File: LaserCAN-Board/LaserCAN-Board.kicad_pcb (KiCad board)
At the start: 4 copper layers, 25 x 25 mm, 48 parts, among them J2 TC2050-IDC-NL, U1 NCP730BMT330TBG, U2 VL53L1CXV0FY1, U3 M24C64-RMN6TP, U4 STM32F103C8Tx, U5 USBLC6-2P6, U6 SN65HVD230, U7 USBLC6-2P6, U8 AP62200TWU-7

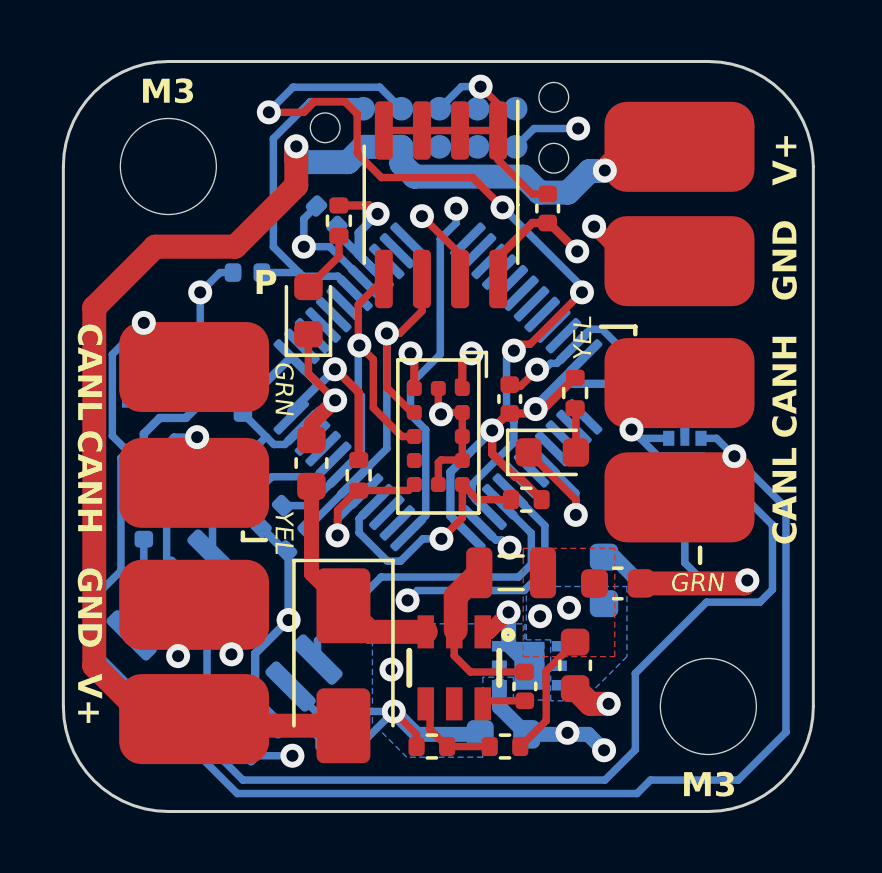
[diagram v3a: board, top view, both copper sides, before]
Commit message: Add new power regulation, completely re-route board to accomodate
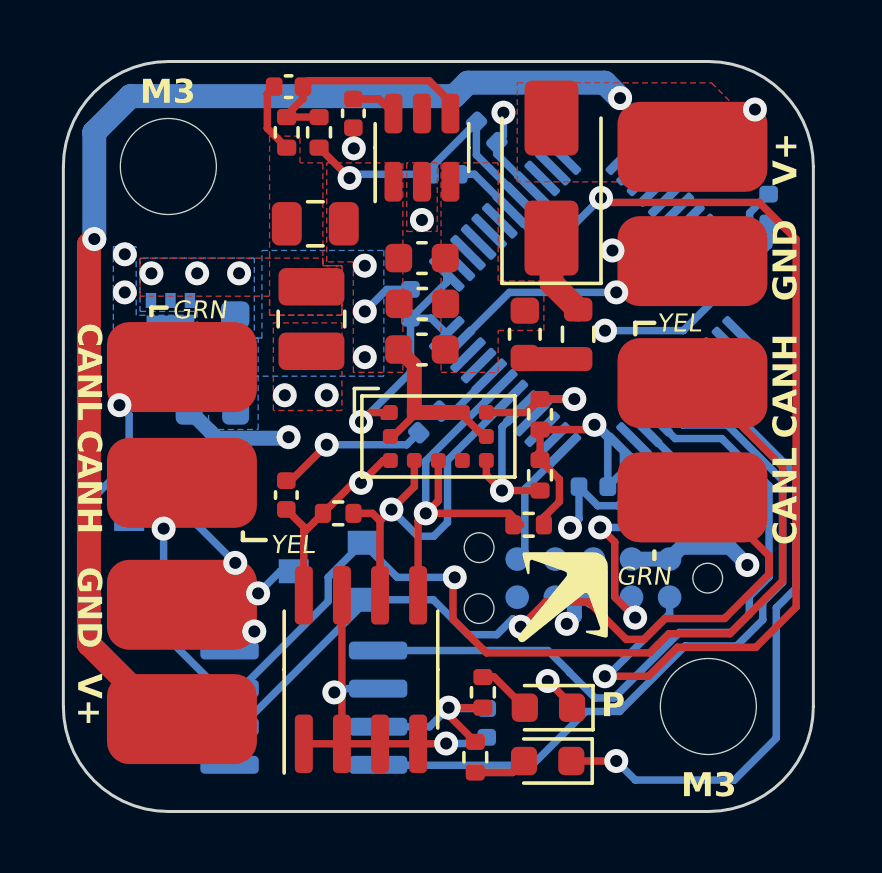
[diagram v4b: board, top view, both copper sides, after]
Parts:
- removed C10, C11, C14: 100n, Capacitor_SMD:C_0402_1005Metric
- removed C15: 10uF, Capacitor_SMD:C_0603_1608Metric
- removed L1: 4.7uH, Inductor_SMD:L_0805_2012Metric
- removed U5, U7: USBLC6-2P6, Package_TO_SOT_SMD:SOT-666
- removed U8: AP62200TWU-7, AP62200TWU-7:TSOT-26_L2.9-W1.6-P0.95-LS2.8-BL
- added C16: 10uF, Capacitor_SMD:C_0603_1608Metric, F.Cu at (132.0, 106.6)
- added C17: 10uF, Capacitor_SMD:C_0603_1608Metric, F.Cu at (132.0, 108.1)
- added C18: 100n, Capacitor_SMD:C_0402_1005Metric, F.Cu at (129.7, 101.7)
- added C19: 22uF, Capacitor_SMD:C_0805_2012Metric, F.Cu at (128.4, 105.4)
- added D4: PESD1CAN,215, PESD1CAN:SOT-23_L2.9-W1.3-P1.90-LS2.4-BR, B.Cu at (123.3, 114.3)
- added D5: PESD1CAN,215, PESD1CAN:SOT-23_L2.9-W1.3-P1.90-LS2.4-BR, B.Cu at (128.8, 117.0)
- added FB1: BLM18AG102SN1D, Inductor_SMD:L_0603_1608Metric, F.Cu at (135.4, 109.1)
- added L2: 22uH, Inductor_SMD:L_1008_2520Metric, F.Cu at (128.3, 108.6)
- added R9: 4.7 100mW, Resistor_SMD:R_0603_1608Metric, F.Cu at (137.2, 109.1)
- added U9: TPS54202DDC, Package_TO_SOT_SMD:SOT-23-6, F.Cu at (132.0, 102.9)
- C13: value 10uF -> 33pF; footprint Capacitor_SMD:C_0603_1608Metric -> Capacitor_SMD:C_0402_1005Metric
- C8: moved to B.Cu
- D1: value D_Schottky -> SS14
- G***, R3, R4: moved to F.Cu
- R2: value 41k 1% -> 100k
- R8: value 10k 1% -> 18.2k
- moved R2 21.7 mm to (127.4, 102.4), turned to 90 degrees
- moved R8 20.8 mm to (128.5, 102.4), turned to -90 degrees
- moved C13 19.9 mm to (127.5, 100.8)
- moved J2 19.2 mm to (140.2, 117.9), turned to 90 degrees
- moved C7 18.6 mm to (143.5, 104.9), turned to 90 degrees
- moved D1 17.7 mm to (136.3, 103.9), turned to 90 degrees
- moved R7 16.4 mm to (134.0, 121.0), turned to 90 degrees
- moved U1 16.4 mm to (123.6, 109.0), turned to 180 degrees
- moved U3 15.7 mm to (129.9, 120.3), turned to 90 degrees
- moved D3 15.5 mm to (136.2, 121.5), turned to 180 degrees
- moved C1 14.7 mm to (125.7, 109.2), turned to -90 degrees
- moved G*** 14.6 mm to (136.7, 117.9), turned to 0 degrees
- moved C3 14.5 mm to (125.0, 111.6), turned to 0 degrees
- moved C2 12.9 mm to (127.4, 114.5)
- moved R6 12.6 mm to (133.7, 123.2)
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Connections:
- net +3V9 renamed /3V87
- C12 pad 1: Net-(D1-K) -> /PWR_IN_FILT
- C13 pad 2: GND -> Net-(U9-FB)
- R2 pad 2: Net-(U8-FB) -> Net-(U9-FB)
- R8 pad 1: Net-(U8-FB) -> Net-(U9-FB)
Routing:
- net /NRST: track 12.0 -> 36.1 mm, vias 0 -> 2
- net /SWDIO: track 28.6 -> 9.43 mm, vias 4 -> 2
- net /STATUS_LED: track 5.05 -> 21.4 mm
- net /SWCLK: track 19.4 -> 4.26 mm, vias 2 -> 0
- net +12V: track 45.8 -> 60.1 mm, vias 2 -> 4
- net +3V3: track 62.7 -> 48.6 mm, vias 10 -> 7
- net /CAN_TX: track 11.3 -> 23.5 mm
- net GND: track 88.0 -> 77.2 mm, vias 16 -> 17
- net /CANL: track 50.9 -> 40.6 mm
- net Net-(U9-FB): track 0.00 -> 8.08 mm
- net /CAN_RX: track 17.0 -> 24.7 mm, vias 2 -> 0
- net Net-(U8-SW): track 5.62 -> 0.00 mm
- net /CANH: track 45.2 -> 40.0 mm
- net Net-(D1-K): track 7.53 -> 2.75 mm
- net /TOF_SHUT: track 8.65 -> 4.81 mm
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- added copper zone on F.Cu, net +12V
- added copper zone on F.Cu, net /BUCK_SW
- added copper zone on In2.Cu, net /BUCK_SW
- added copper zone on F.Cu, net /PWR_IN_FILT
- added copper zone on F.Cu, net GND
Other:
- board text added: "LaserCAN Rev. 4"
- board text removed: "LaserCAN Rev. 3.1"

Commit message: Modify the routing a little bit
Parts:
- moved C5 1.05 mm to (133.1, 102.6), turned to 0 degrees
- moved C4 0.54 mm to (132.3, 104.1)
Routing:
- net +3V3: track 48.6 -> 49.4 mm
- net GND: track 77.2 -> 76.7 mm

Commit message: Rev 4 updates
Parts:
- removed D5: PESD1CAN,215, PESD1CAN:SOT-23_L2.9-W1.3-P1.90-LS2.4-BR
- removed R1, R5: 10k, Resistor_SMD:R_0402_1005Metric
- removed R3, R4: 4k7, Resistor_SMD:R_0402_1005Metric
- added C10: 22uF, Capacitor_SMD:C_0603_1608Metric, F.Cu at (128.5, 104.2)
- added C11: 22uF, Capacitor_SMD:C_0603_1608Metric, F.Cu at (128.4, 105.8)
- added C14: 100n, Capacitor_SMD:C_0402_1005Metric, F.Cu at (130.3, 114.7)
- added C15: 100n, Capacitor_SMD:C_0402_1005Metric, F.Cu at (129.1, 112.7)
- added D6: SMF12A, Diode_SMD:D_SOD-123F, F.Cu at (137.0, 104.1)
- added NT1: NetTie_2, NetTie:NetTie-2_SMD_Pad0.5mm, F.Cu at (129.2, 103.1)
- added NT2: NetTie_2, NetTie:NetTie-2_SMD_Pad2.0mm, F.Cu at (137.7, 107.5)
- added RN1: YC164-JR-074K7L, Resistor_SMD:R_Array_Convex_4x0603, B.Cu at (131.0, 117.8)
- C19: value 22uF -> 10uF; footprint Capacitor_SMD:C_0805_2012Metric -> Capacitor_SMD:C_0603_1608Metric; moved to B.Cu
- D1: value SS14 -> ZLLS400TA; footprint Diode_SMD:D_SMA -> Diode_SMD:D_SOD-323
- D4: value PESD1CAN,215 -> ESDCAN24-2BLY; footprint PESD1CAN:SOT-23_L2.9-W1.3-P1.90-LS2.4-BR -> Package_TO_SOT_SMD:SOT-23
- U1: value NCP730BMT330TBG -> TPS7A2033PDBVR; footprint NCP730BMT330TBG:WDFN-6_L2.0-W2.0-P0.65-BL-EP-1 -> Package_TO_SOT_SMD:SOT-23-5
- moved C19 17.6 mm to (122.1, 121.8), turned to 135 degrees
- moved D2 8.89 mm to (142.5, 117.1)
- moved D3 8.83 mm to (127.6, 119.5), turned to 90 degrees
- moved R6 8.50 mm to (139.8, 117.2), turned to 0 degrees
- moved R7 7.22 mm to (127.9, 117.1), turned to 180 degrees
- moved C8 6.89 mm to (129.8, 114.7), turned to -45 degrees
- moved J2 6.85 mm to (136.0, 123.2)
- moved C9 6.16 mm to (128.0, 122.6), turned to -135 degrees
- moved G*** 5.69 mm to (133.4, 122.5)
- moved C7 5.63 mm to (141.7, 110.2), turned to 135 degrees
- moved C2 5.21 mm to (129.8, 119.1)
- moved R10 5.13 mm to (128.8, 115.8), turned to 0 degrees
- moved C6 4.84 mm to (135.9, 118.7)
- moved U4 4.84 mm to (135.9, 112.6)
- moved U3 4.81 mm to (134.3, 118.2), turned to 180 degrees
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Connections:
- C19 pad 1: /3V87 -> +3V3
- J4 pad 1: GND -> GNDPWR
- J5 pad 1: GND -> GNDPWR
- R8 pad 2: GND -> Net-(NT1-Pad1)
- U1 pad 1: +3V3 -> /3V87
- U1 pad 3: GND -> /3V87
- U1 pad 4: /3V87 -> unconnected-(U1-NC-Pad4)
- U1 pad 5: unconnected-(U1-PG-Pad5) -> +3V3
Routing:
- net GND: track 76.7 -> 5.66 mm, vias 17 -> 34
- net GNDPWR: track 0.00 -> 40.4 mm, vias 0 -> 7
- net +3V3: track 49.4 -> 82.0 mm, vias 7 -> 6
- net /STATUS_LED: track 21.4 -> 6.41 mm
- net /CAN_TX: track 23.5 -> 17.1 mm, vias 0 -> 2
- net +12V: track 59.8 -> 65.8 mm, vias 4 -> 10
- net /I2C_SDA: track 13.3 -> 8.64 mm
- net /TOF_SHUT: track 4.81 -> 8.33 mm
- net /I2C_SCL: track 13.4 -> 10.1 mm
- net /SWDIO: track 9.43 -> 11.9 mm
- net /CAN_RX: track 24.7 -> 22.6 mm, vias 0 -> 2
- net /SWCLK: track 4.26 -> 6.16 mm
- net Net-(U4-BOOT0): track 2.11 -> 3.38 mm
- net Net-(D1-K): track 2.75 -> 1.53 mm
- net /CANH: track 40.0 -> 41.1 mm
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- added copper zone on In1.Cu, net /BUCK_SW
- added copper zone on In2.Cu, net GND
- added copper zone on F.Cu, net GNDPWR
- removed copper zone on In2.Cu, net +3V3
- removed copper zone on In2.Cu, net /BUCK_SW

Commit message: Rev 4 - more updates
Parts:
- added C20: 33pF, Capacitor_SMD:C_0402_1005Metric, B.Cu at (136.7, 102.7)
- added C21: 33pF, Capacitor_SMD:C_0402_1005Metric, B.Cu at (130.8, 101.9)
- added Y1: 8MHz 20pF, Crystal:Crystal_SMD_3225-4Pin_3.2x2.5mm, B.Cu at (134.0, 102.6)
- C13: moved to B.Cu
- D6: value SMF12A -> SMF15CA; footprint Diode_SMD:D_SOD-123F -> Diode_SMD:D_SMF
- moved C10 4.47 mm to (128.5, 108.7)
- moved C11 4.42 mm to (128.5, 110.2)
- moved L2 2.64 mm to (128.4, 105.9), turned to -90 degrees
- moved NT1 1.49 mm to (130.6, 103.6)
- moved C1 1.47 mm to (128.7, 109.3), turned to -90 degrees
- moved C13 1.09 mm to (127.9, 101.9)
- moved U1 0.85 mm to (125.5, 109.5), turned to 180 degrees
- moved C18 0.63 mm to (129.7, 102.4)
- moved C3 0.36 mm to (122.5, 109.4), turned to -90 degrees
- moved C19 0.23 mm to (122.3, 121.8)
- moved C4 0.13 mm to (131.2, 108.0)
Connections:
- U4 pad 5: unconnected-(U4-PD0-Pad5) -> Net-(U4-PD0)
- U4 pad 6: unconnected-(U4-PD1-Pad6) -> Net-(U4-PD1)
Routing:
- net /CANL: track 41.4 -> 26.8 mm
- net Net-(U4-PD1): track 0.00 -> 14.3 mm
- net Net-(U4-PD0): track 0.00 -> 13.8 mm
- net /CANH: track 41.1 -> 28.7 mm, vias 2 -> 3
- net +3V3: track 82.0 -> 88.8 mm, vias 6 -> 7
- net /3V87: track 2.36 -> 8.19 mm
- net GND: track 5.66 -> 10.5 mm, vias 34 -> 72
- net Net-(NT1-Pad1): track 0.00 -> 2.15 mm, vias 0 -> 2
- net /CAN_RX: track 22.6 -> 20.5 mm
- net /SWDIO: track 11.9 -> 12.4 mm
- net /BUCK_SW: track 0.90 -> 1.13 mm, vias 9 -> 8
- net Net-(U9-FB): track 7.59 -> 7.79 mm, vias 0 -> 1

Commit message: Rev 4 Complete, barring any more review
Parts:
- added Q1: Si2309CDS-T1-GE3, SI2309CDS-T1-GE3:SOT-23_L2.9-W1.3-P1.90-LS2.4-BR, F.Cu at (136.1, 102.3)
- added R1: 10k, Resistor_SMD:R_0402_1005Metric, B.Cu at (137.8, 102.7)
- D1: value ZLLS400TA -> 12V; footprint Diode_SMD:D_SOD-323 -> Diode_SMD:D_SOD-523; moved to B.Cu
- moved D1 3.71 mm to (136.4, 105.4), turned to 0 degrees
- moved D6 2.39 mm to (137.1, 106.5)
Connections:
- D1 pad 2: +12V -> Net-(D1-A)
- U4 pad 4: unconnected-(U4-PC15-Pad4) -> GND
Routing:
- net Net-(D1-A): track 0.00 -> 7.98 mm, vias 0 -> 1
- net GND: track 10.5 -> 8.93 mm
- net Net-(D1-K): track 1.53 -> 2.97 mm, vias 0 -> 1
